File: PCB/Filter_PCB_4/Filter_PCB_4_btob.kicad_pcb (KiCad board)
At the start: 4 copper layers, 36.6 x 8.9 mm, 45 parts, among them J1 Conn_Coaxial, J2 Conn_Coaxial, J3 Conn_01x06_Male, U1 MCP4728

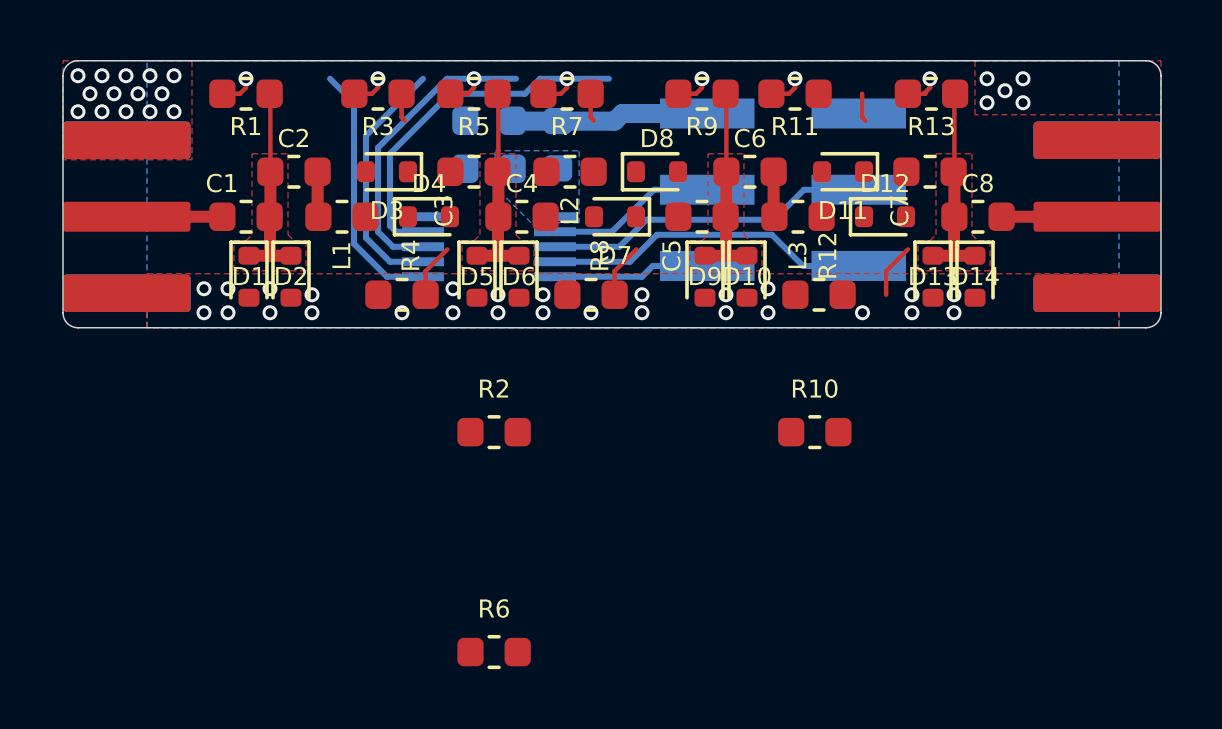
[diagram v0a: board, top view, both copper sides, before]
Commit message: PCB updated
resistori 0603 sostituiti da resistori 0402
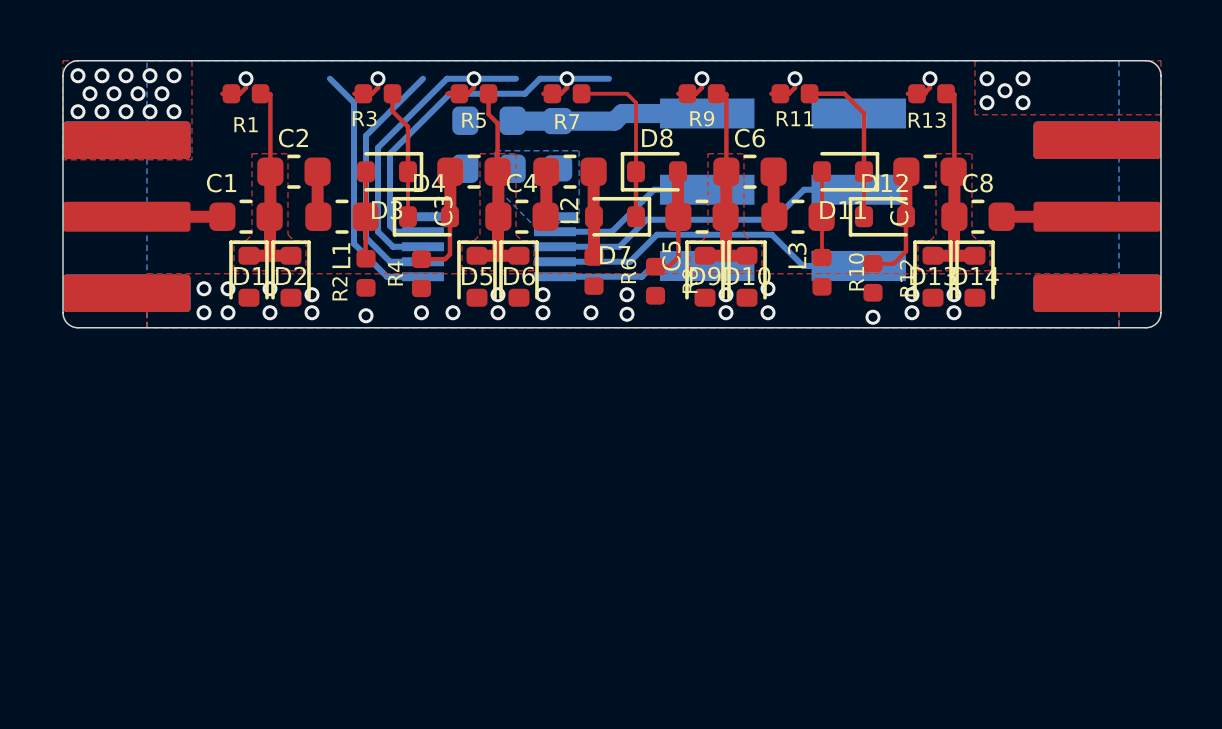
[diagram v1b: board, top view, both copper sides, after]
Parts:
- R1, R10, R11, R12, R13, R2, R3, R4, R5, R6, R7, R8, R9: footprint Resistor_SMD:R_0603_1608Metric -> Resistor_SMD:R_0402_1005Metric
- moved R6 13.1 mm to (163.4, 103.1), turned to 270 degrees
- moved R2 6.80 mm to (155.8, 103.2), turned to 270 degrees
- moved R10 5.34 mm to (171.0, 103.2), turned to 270 degrees
- moved R8 2.20 mm to (165.4, 103.5), turned to 270 degrees
- moved R12 1.88 mm to (172.7, 103.3), turned to 270 degrees
- moved R4 0.96 mm to (157.7, 103.2), turned to 270 degrees
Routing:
- net /RF/res1/Vd+: track 0.95 -> 5.74 mm
- net /RF/res2/Vd+: track 0.95 -> 5.53 mm
- net /RF/res0/Vd+: track 0.95 -> 4.31 mm
- net /RF/res0/Vd-L: track 0.00 -> 2.91 mm
- net /RF/res2/Vd-L: track 0.00 -> 2.88 mm
- net /RF/res1/Vd-L: track 0.00 -> 2.85 mm
- net /RF/inv3/In: track 1.81 -> 3.93 mm
- net /RF/inv1/In: track 1.81 -> 3.77 mm
- net /RF/inv2/In: track 1.81 -> 3.74 mm
- net /RF/res1/In: track 0.04 -> 1.55 mm

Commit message: pcb4 board update
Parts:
- moved R11 2.22 mm to (171.9, 98.5)
- moved R7 2.22 mm to (164.3, 98.5)
- moved R9 1.84 mm to (168.3, 98.5), turned to 180 degrees
- moved R1 1.84 mm to (153.1, 98.5), turned to 180 degrees
- moved R3 1.39 mm to (156.7, 98.5)
- moved R5 1.33 mm to (159.7, 98.5)
- moved R13 1.32 mm to (174.9, 98.5)
- moved J3 0.85 mm to (169.1, 101.0)
- moved C9 0.60 mm to (159.9, 98.7)
- moved U1 0.60 mm to (159.9, 102.9)
- moved C10 0.60 mm to (159.9, 100.3)
- moved L4 0.60 mm to (162.2, 99.5)
- moved R12 0.34 mm to (173.0, 103.2)
- moved R8 0.25 mm to (165.4, 103.2)
- moved R6 0.08 mm to (163.4, 103.2)
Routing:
- net /RF/res1/Vd+: track 5.74 -> 2.81 mm
- net /RF/V1: track 23.8 -> 26.7 mm
- net /RF/V2: track 19.1 -> 22.0 mm, vias 2 -> 3
- net /RF/res2/Vd+: track 5.53 -> 2.81 mm
- net VDD: track 6.60 -> 8.33 mm
- net /RF/res0/Vd+: track 4.31 -> 2.81 mm
- net /RF/inv1/Vd: track 6.94 -> 5.52 mm
- net /RF/inv3/Vd: track 6.83 -> 5.52 mm
- net /RF/inv0/Vd: track 6.83 -> 5.52 mm
- net /RF/inv2/Vd: track 6.83 -> 5.53 mm
- net /RF/V0: track 30.6 -> 31.8 mm
- net /DAC/~LDAC: track 11.8 -> 10.8 mm
- net /DAC/SDA: track 11.8 -> 10.9 mm
- net /DAC/RDY: track 6.12 -> 5.22 mm
- net /DAC/SCL: track 6.55 -> 5.65 mm
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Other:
- board size 36.6 x 8.9 mm -> 36.6 x 7.4 mm
